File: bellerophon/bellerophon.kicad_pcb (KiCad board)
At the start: 2 copper layers, 22 parts, among them IC1 L7805ACV, IC2 Adafruit_MPL3115A2, J1 Battery, J2 Switch, J3 Screw_Terminal_01x04, Q1 IRLB8721PBF, Q2 IRLB8721PBF, U1 Adafruit_ICM20948, U2 Teensy4.0, U3 Adafruit SPI Flash SD Card

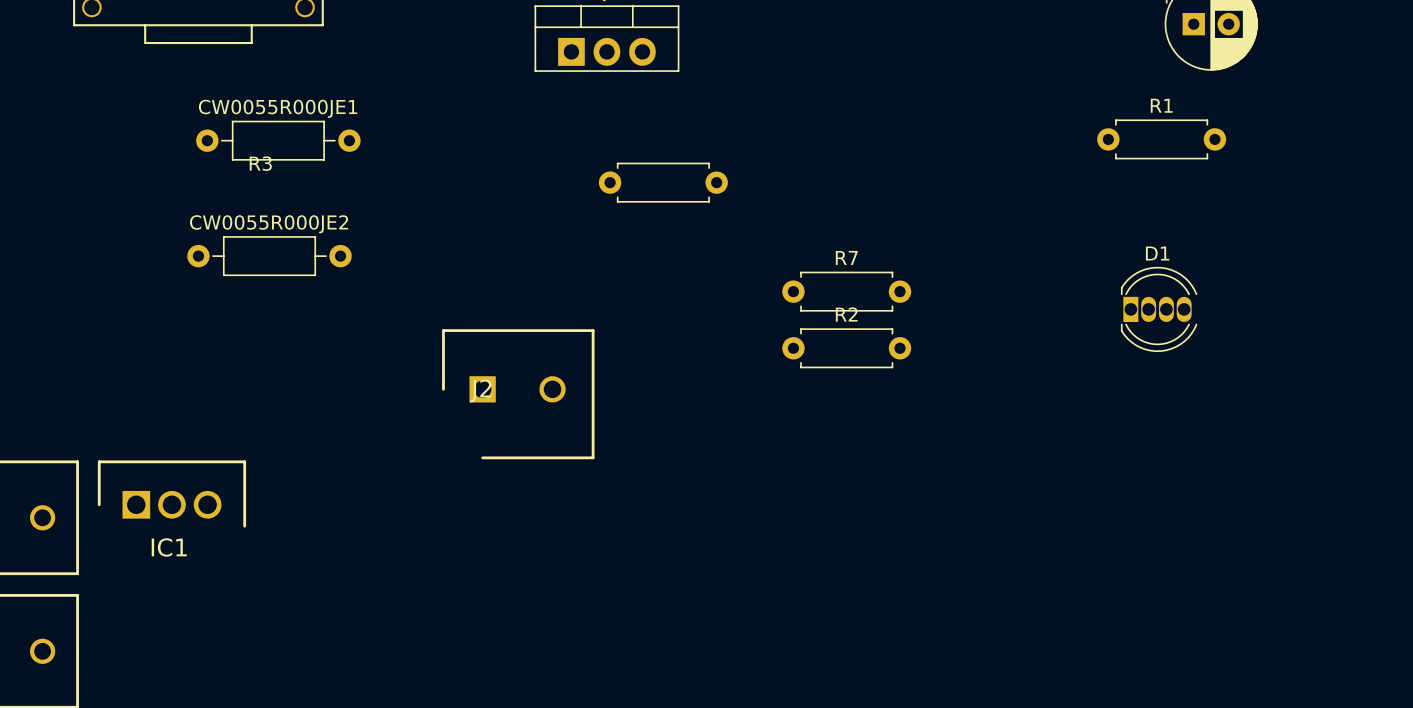
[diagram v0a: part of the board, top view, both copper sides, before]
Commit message: add bulky resistor footprints
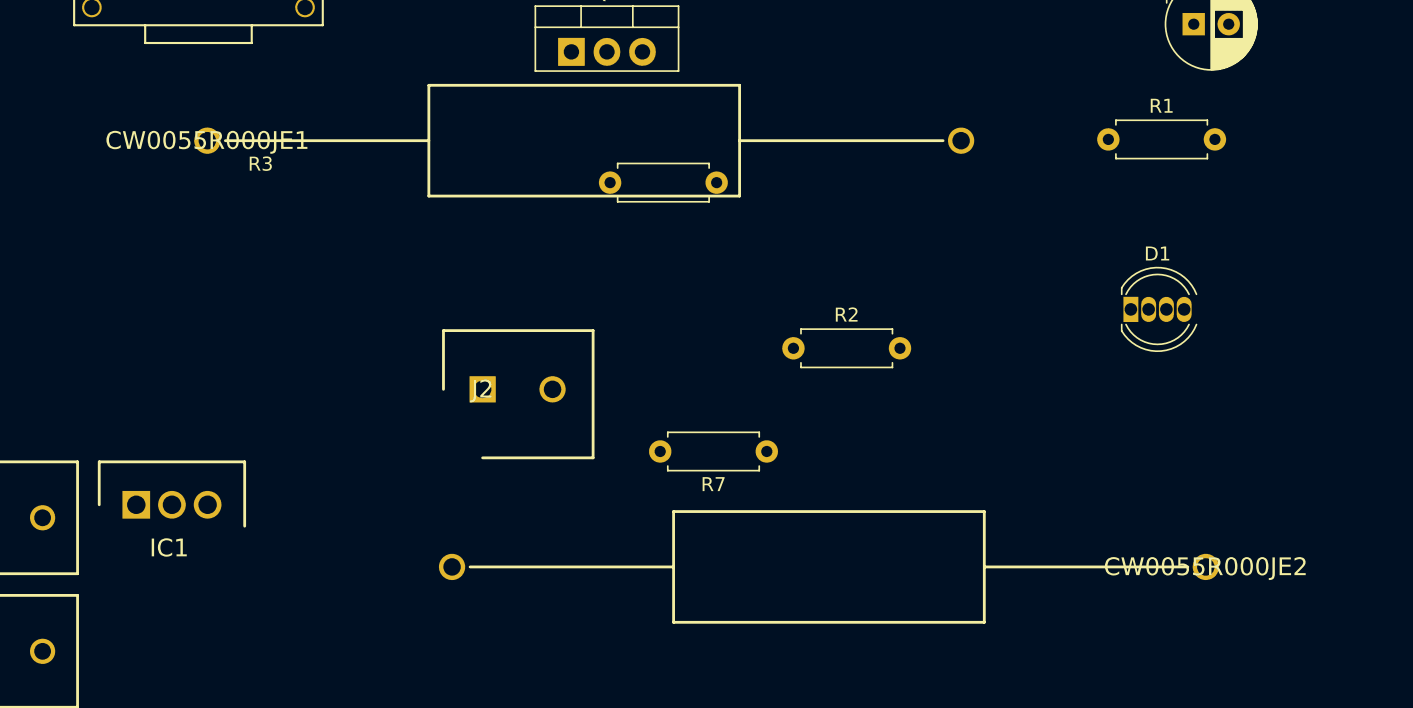
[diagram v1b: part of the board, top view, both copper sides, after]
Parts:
- CW0055R000JE1, CW0055R000JE2: footprint Resistor_THT:R_Axial_DIN0207_L6.3mm_D2.5mm_P10.16mm_Horizontal -> RS-Components:RESAD5390W107L2222D792
- moved CW0055R000JE2 75.4 mm to (225.1, 132.7), turned to 180 degrees
- moved R7 11.6 mm to (193.7, 124.5), turned to 180 degrees

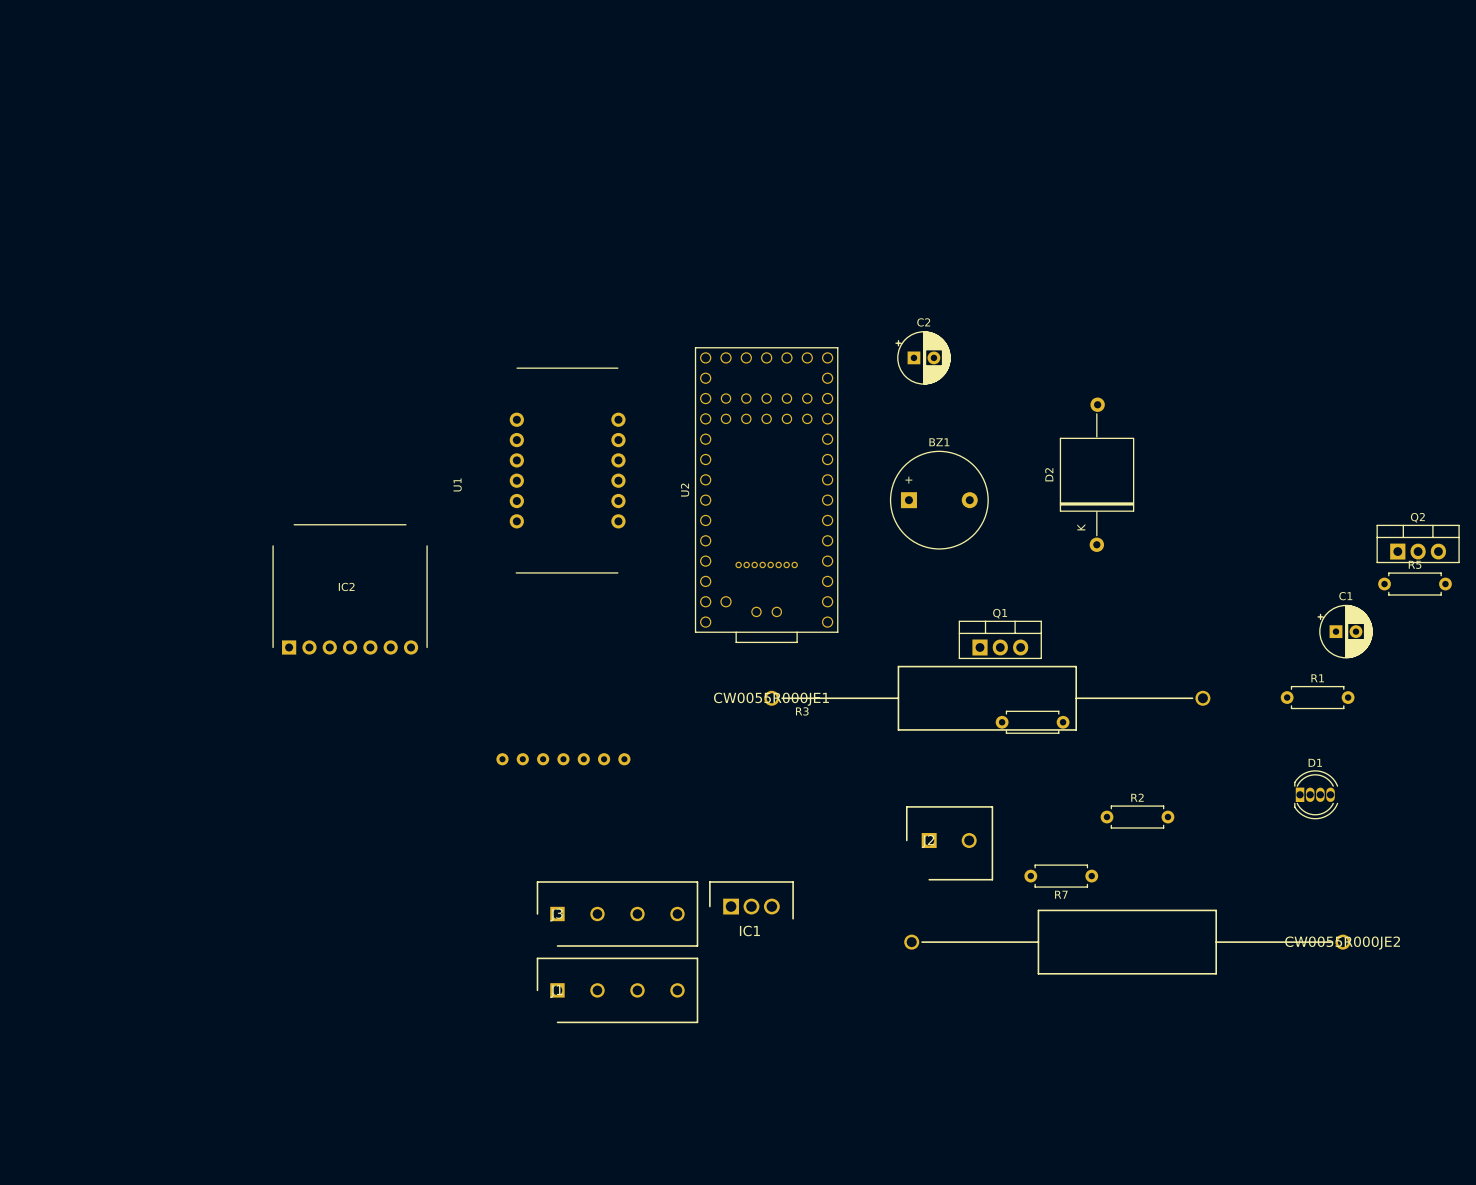
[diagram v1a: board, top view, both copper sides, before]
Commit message: change teensy footprint to THT, change some resistors, layed out components and boardcut in pcbnew
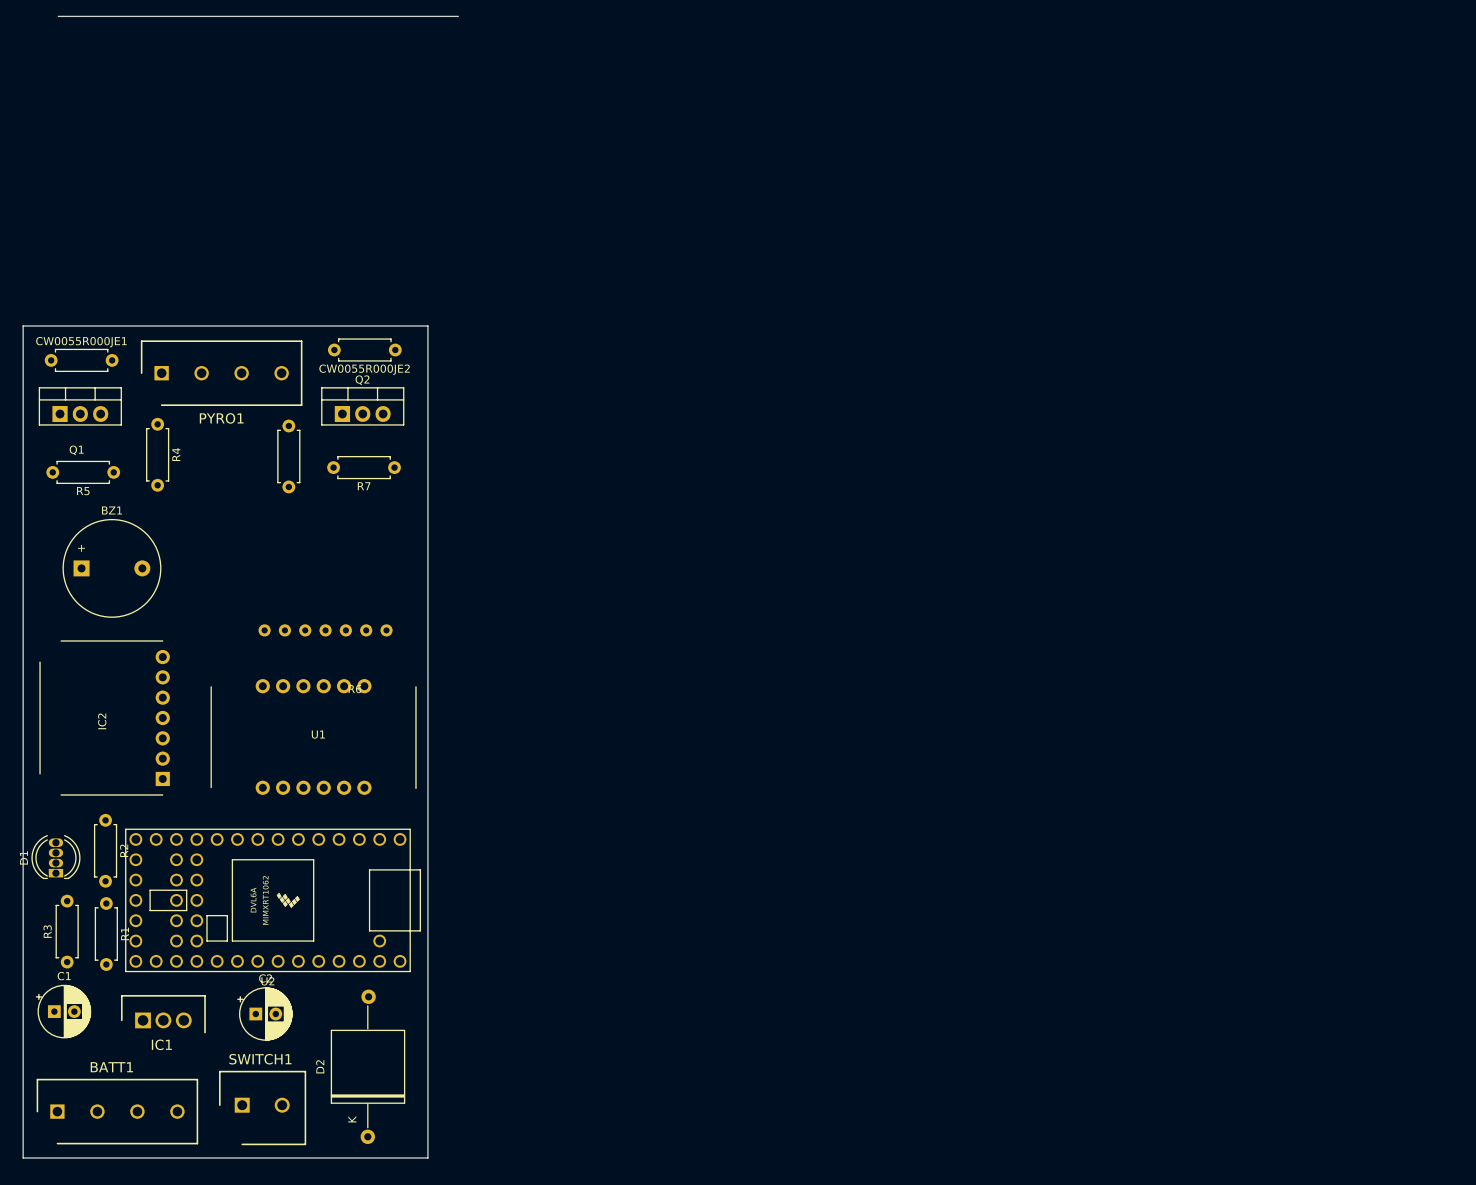
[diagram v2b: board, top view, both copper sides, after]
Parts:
- added R4: 470 ohms, Resistor_THT:R_Axial_DIN0207_L6.3mm_D2.5mm_P7.62mm_Horizontal, F.Cu at (76.9, 68.0)
- added R6: 470 ohms, Resistor_THT:R_Axial_DIN0207_L6.3mm_D2.5mm_P7.62mm_Horizontal, F.Cu at (93.3, 68.2)
- BATT1: renamed from J1; value Battery -> Screw_Terminal_01x04
- CW0055R000JE1, CW0055R000JE2: footprint RS-Components:RESAD5390W107L2222D792 -> Resistor_THT:R_Axial_DIN0207_L6.3mm_D2.5mm_P7.62mm_Horizontal
- SWITCH1: renamed from J2; value Switch -> Screw_Terminal_01x04
- U2: footprint teensy:Teensy40_SMT -> teensy:Teensy40
- moved C1 167.1 mm to (64.0, 141.4)
- moved R5 159.5 mm to (71.4, 74.0), turned to 180 degrees
- moved D1 155.8 mm to (64.2, 124.1), turned to 90 degrees
- moved R1 149.8 mm to (70.5, 127.9), turned to -90 degrees
- moved CW0055R000JE2 139.7 mm to (106.6, 58.7)
- moved Q2 133.0 mm to (100.0, 66.7)
- moved R2 125.2 mm to (70.4, 117.5), turned to -90 degrees
- moved R3 120.7 mm to (65.6, 135.2), turned to 90 degrees
- moved Q1 118.6 mm to (64.7, 66.7)
- moved D2 117.4 mm to (103.2, 148.3)
- moved C2 116.2 mm to (89.2, 141.7)
- moved BZ1 103.8 mm to (67.4, 86.0)
- moved R7 101.0 mm to (106.5, 73.4)
- moved CW0055R000JE1 99.5 mm to (63.6, 60.0)
- moved SWITCH1 92.0 mm to (87.5, 153.1)
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- renumbered J3 to PYRO1
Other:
- board outline added: 54.4 x 142.7 mm

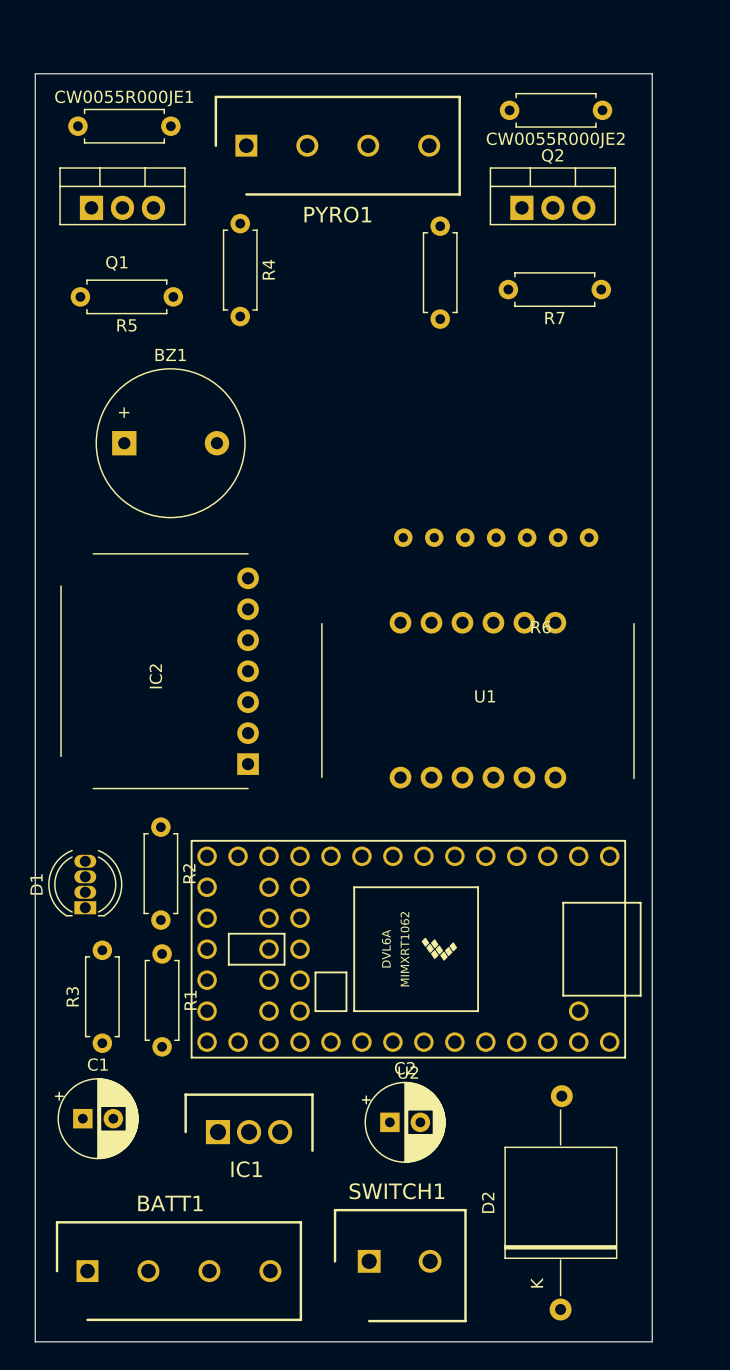
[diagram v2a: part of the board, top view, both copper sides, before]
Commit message: change some teensy pins, reorganise component placement
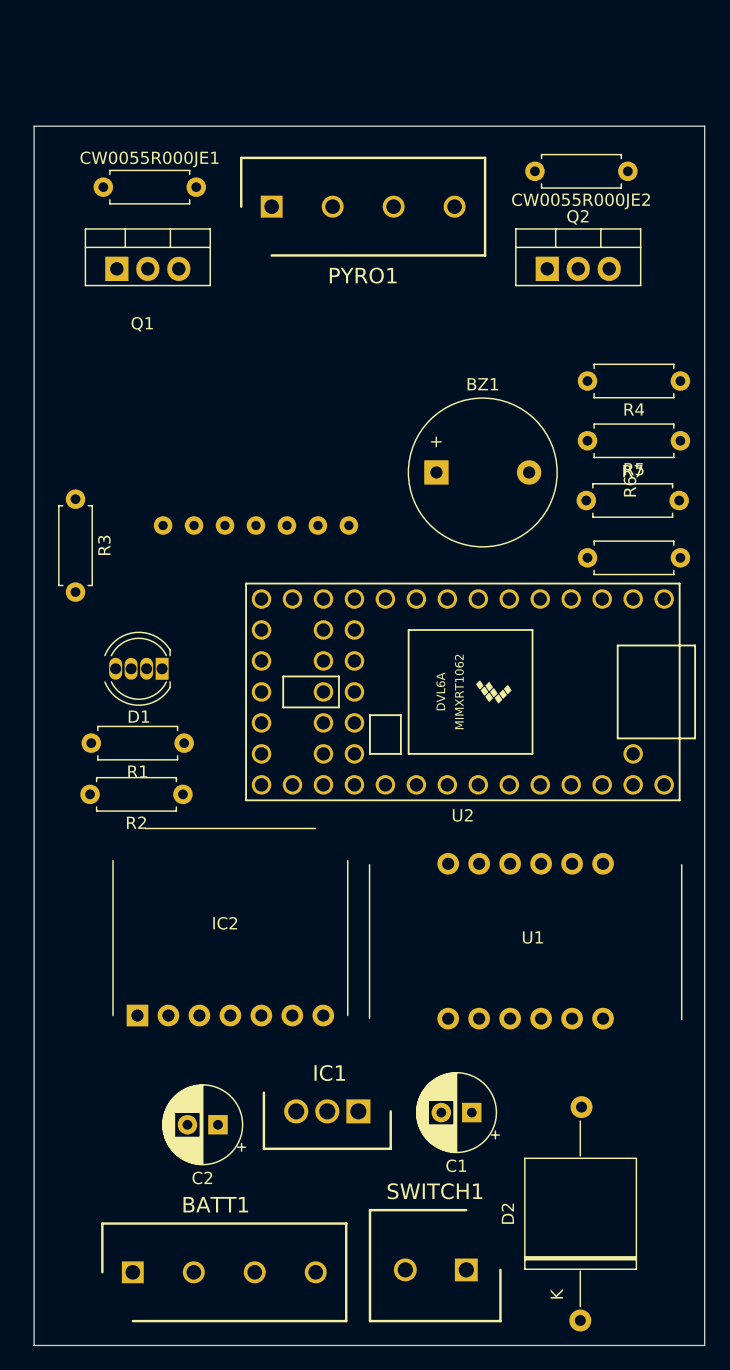
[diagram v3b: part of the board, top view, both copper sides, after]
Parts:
- moved R3 44.7 mm to (63.4, 90.6), turned to -90 degrees
- moved R5 43.2 mm to (113.0, 85.8)
- moved R4 38.3 mm to (113.0, 80.9), turned to 180 degrees
- moved R6 33.6 mm to (113.0, 95.4), turned to 180 degrees
- moved C1 31.9 mm to (95.9, 140.9), turned to 180 degrees
- moved BZ1 25.7 mm to (93.0, 88.4)
- moved IC2 25.1 mm to (75.7, 130.2), turned to 0 degrees
- moved U2 21.6 mm to (95.2, 106.4)
- moved D1 20.6 mm to (70.5, 104.5), turned to 180 degrees
- moved U1 20.2 mm to (102.1, 140.1)
- moved U3 19.7 mm to (78.2, 86.4)
- moved R1 17.4 mm to (72.3, 110.6), turned to 180 degrees
- moved R7 17.3 mm to (105.3, 90.7), turned to 0 degrees
- moved C2 14.1 mm to (75.1, 141.9), turned to 180 degrees
- moved IC1 11.6 mm to (86.6, 140.8), turned to 180 degrees
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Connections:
- U2 pad 10: BZR -> RGB3
- U2 pad 13: /MISO -> /MOSI
- U2 pad 14: /MOSI -> /MISO
- U2 pad 21: unconnected-(U2-Pad21) -> RGB1
- U2 pad 22: unconnected-(U2-Pad22) -> RGB2
- U2 pad 23: unconnected-(U2-Pad23) -> MPL3115A2 SCL
- U2 pad 24: unconnected-(U2-Pad24) -> MPL3115A2 SDA
- U2 pad 35: MPL3115A2 SCL -> unconnected-(U2-Pad35)
- U2 pad 36: MPL3115A2 SDA -> unconnected-(U2-Pad36)
- U2 pad 7: RGB1 -> unconnected-(U2-Pad7)
- U2 pad 8: RGB2 -> unconnected-(U2-Pad8)
- U2 pad 9: RGB3 -> BZR
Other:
- board size 54.4 x 142.7 mm -> 55 x 143 mm
